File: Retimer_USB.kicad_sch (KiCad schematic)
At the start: 24 parts, among them IC1 PI2EQX22024XEAEX

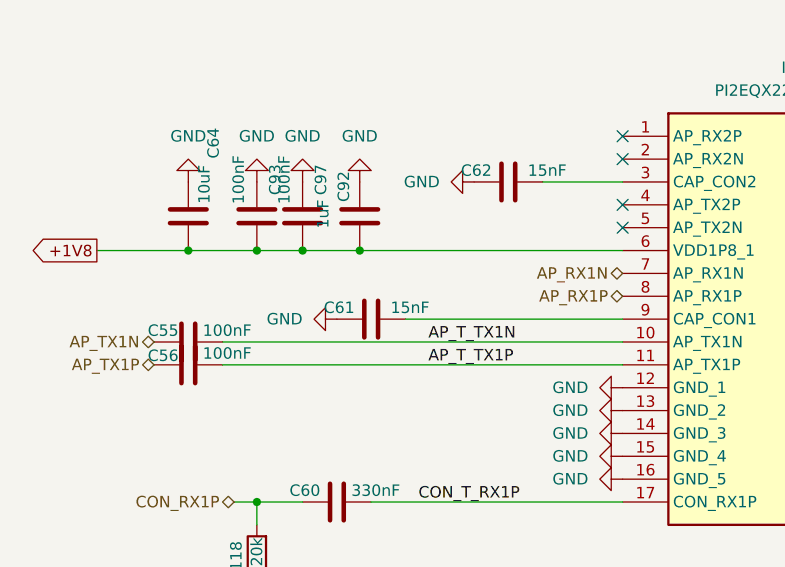
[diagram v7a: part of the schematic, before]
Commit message: added 100nF cap to rx of ucb
added 100nF cap to rx of ucb
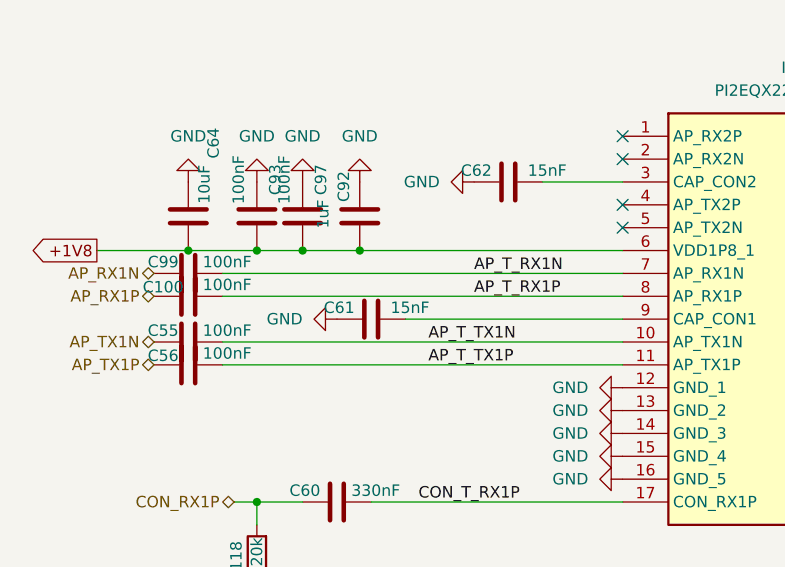
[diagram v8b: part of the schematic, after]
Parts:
- added C100, C99: 100nF, Capacitor_SMD:C_0201_0603Metric, symbol Device:C
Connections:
- net AP_RX1N: now also C99.2; no longer IC1.7 (AP_RX1N)
- net AP_RX1P: now also C100.2; no longer IC1.8 (AP_RX1P)
- new net AP_T_RX1N: C99.1, IC1.7 (AP_RX1N)
- new net AP_T_RX1P: C100.1, IC1.8 (AP_RX1P)
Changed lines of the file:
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@@
 	(wire
 		(pts
+			(xy 97.79 85.09) (xy 142.24 85.09)
+		)
+		(stroke
+			(width 0)
+			(type default)
+		)
+	)
+	(wire
+		(pts
 			(xy 180.34 69.85) (xy 195.58 69.85)
 		)
@@
 	(wire
 		(pts
+			(xy 97.79 87.63) (xy 142.24 87.63)
+		)
+		(stroke
+			(width 0)
+			(type default)
+		)
+	)
+	(wire
+		(pts
 			(xy 224.79 124.46) (xy 226.06 124.46)
 		)
@@
 		)
 	)
+	(label "AP_T_RX1N"
+		(at 125.73 85.09 0)
+		(effects
+			(font
+				(size 1.27 1.27)
+			)
+			(justify left bottom)
+		)
+	)
 	(label "CON_T_RX1P"
 		(at 130.81 110.49 180)
@@
 		)
 	)
+	(label "AP_T_RX1P"
+		(at 125.73 87.63 0)
+		(effects
+			(font
+				(size 1.27 1.27)
+			)
+			(justify left bottom)
+		)
+	)
 	(label "CON_T_RX1N"
 		(at 191.77 69.85 180)
@@
 	(hierarchical_label "AP_RX1P"
 		(shape bidirectional)
-		(at 142.24 87.63 180)
+		(at 90.17 87.63 180)
 		(effects
 			(font
@@
 	(hierarchical_label "AP_RX1N"
 		(shape bidirectional)
-		(at 142.24 85.09 180)
+		(at 90.17 85.09 180)
 		(effects
 			(font
@@
 	(symbol
 		(lib_id "Device:C")
+		(at 93.98 85.09 270)
+		(unit 1)
+		(exclude_from_sim no)
+		(in_bom yes)
+		(on_board yes)
+		(dnp no)
+		(property "Reference" "C99"
+			(at 91.186 83.82 90)
+			(effects
+				(font
+					(size 1.27 1.27)
+				)
+			)
+		)
+		(property "Value" "100nF"
+			(at 98.298 83.82 90)
+			(effects
+				(font
+					(size 1.27 1.27)
+				)
+			)
+		)
+		(property "Footprint" "Capacitor_SMD:C_0201_0603Metric"
+			(at 90.17 86.0552 0)
+			(effects
+				(font
+					(size 1.27 1.27)
+				)
+				(hide yes)
+			)
+		)
+		(property "Datasheet" "~"
+			(at 93.98 85.09 0)
+			(effects
+				(font
+					(size 1.27 1.27)
+				)
+				(hide yes)
+			)
+		)
+		(property "Description" "Unpolarized capacitor"
+			(at 93.98 85.09 0)
+			(effects
+				(font
+					(size 1.27 1.27)
+				)
+				(hide yes)
+			)
+		)
+		(property "Part_Number" "GRM033R61C104KE84D"
+			(at 93.98 85.09 0)
+			(effects
+				(font
+					(size 1.27 1.27)
+				)
+				(hide yes)
+			)
+		)
+		(property "LCSC" "C76937"
+			(at 93.98 85.09 0)
+			(effects
+				(font
+					(size 1.27 1.27)
+				)
+				(hide yes)
+			)
+		)
+		(pin "1"
+		)
+		(pin "2"
+		)
+		(instances
+			(project "XG_Mobile_Dock_XT"
+				(path "/f97e6956-ab08-42cb-8fed-03fa58e87f0e/a254375d-80c0-4b18-9fd6-3cbd6a868414"
+					(reference "C99")
+					(unit 1)
+				)
+			)
+		)
+	)
+	(symbol
+		(lib_id "Device:C")
 		(at 241.3 63.5 0)
 		(mirror x)
@@
 					(unit 1)
 				)
+			)
+		)
+	)
+	(symbol
+		(lib_id "Device:C")
+		(at 93.98 87.63 270)
+		(unit 1)
+		(exclude_from_sim no)
+		(in_bom yes)
+		(on_board yes)
+		(dnp no)
+		(property "Reference" "C100"
+			(at 91.186 86.614 90)
+			(effects
+				(font
+					(size 1.27 1.27)
+				)
+			)
+		)
+		(property "Value" "100nF"
+			(at 98.298 86.36 90)
+			(effects
+				(font
+					(size 1.27 1.27)
+				)
+			)
+		)
+		(property "Footprint" "Capacitor_SMD:C_0201_0603Metric"
+			(at 90.17 88.5952 0)
+			(effects
+				(font
+					(size 1.27 1.27)
+				)
+				(hide yes)
+			)
+		)
+		(property "Datasheet" "~"
+			(at 93.98 87.63 0)
+			(effects
+				(font
+					(size 1.27 1.27)
+				)
+				(hide yes)
+			)
+		)
+		(property "Description" "Unpolarized capacitor"
+			(at 93.98 87.63 0)
+			(effects
+				(font
+					(size 1.27 1.27)
+				)
+				(hide yes)
+			)
+		)
+		(property "Part_Number" "GRM033R61C104KE84D"
+			(at 93.98 87.63 0)
+			(effects
+				(font
+					(size 1.27 1.27)
+				)
+				(hide yes)
+			)
+		)
+		(property "LCSC" "C76937"
+			(at 93.98 87.63 0)
+			(effects
+				(font
+					(size 1.27 1.27)
+				)
+				(hide yes)
+			)
+		)
+		(pin "1"
+		)
+		(pin "2"
+		)
+		(instances
+			(project "XG_Mobile_Dock_XT"
+				(path "/f97e6956-ab08-42cb-8fed-03fa58e87f0e/a254375d-80c0-4b18-9fd6-3cbd6a868414"
+					(reference "C100")
+					(unit 1)
+				)
